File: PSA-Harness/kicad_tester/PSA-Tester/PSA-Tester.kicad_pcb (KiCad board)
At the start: 2 copper layers, 35 parts, among them J11 USB_C_Receptacle, SW1 SW_Push, SW2 SW_Push, SW3 SW_Push, U1 MCP23017_SO, U10 ESP32-C3-OLED, U2 MCP23017_SO, U3 MCP23017_SO, U4 MCP23017_SO, U5 MCP23017_SO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

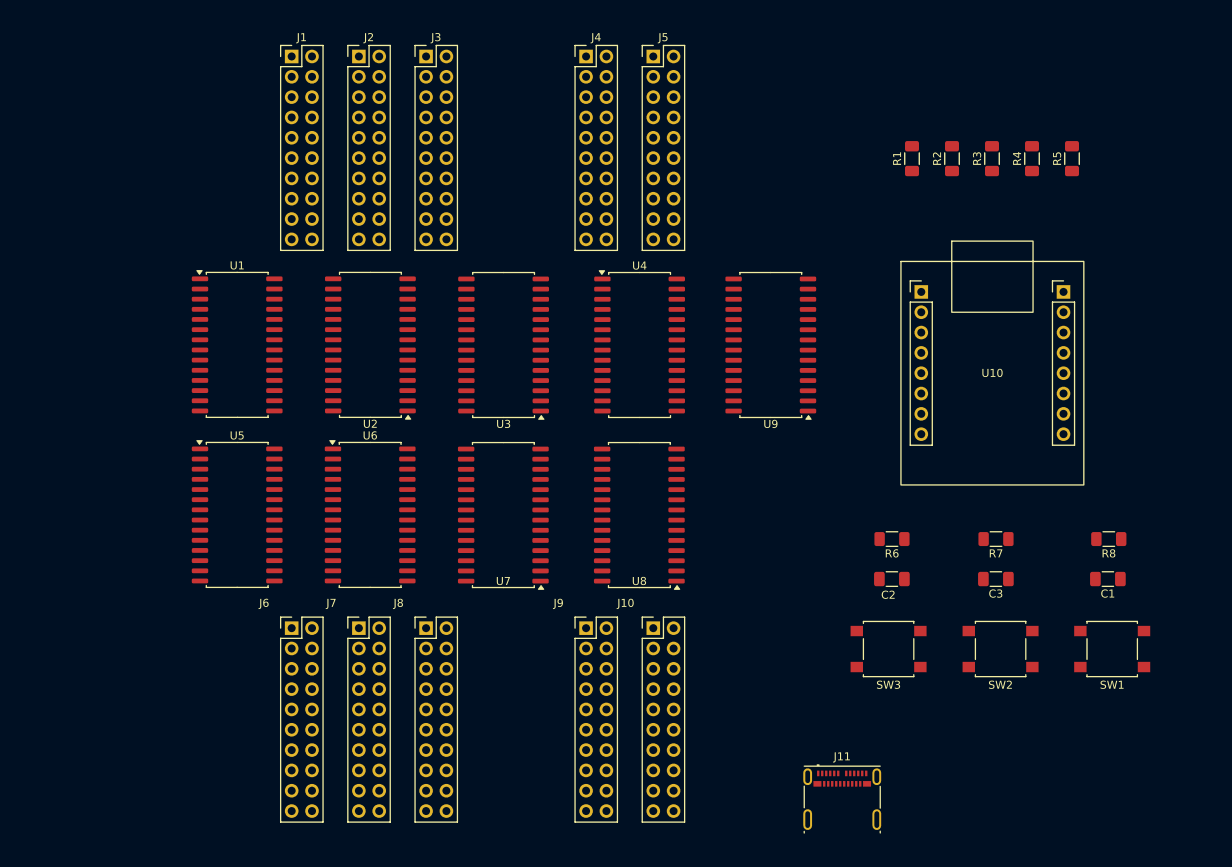
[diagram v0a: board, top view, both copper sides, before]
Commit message: swap mux footprint to DIP-28
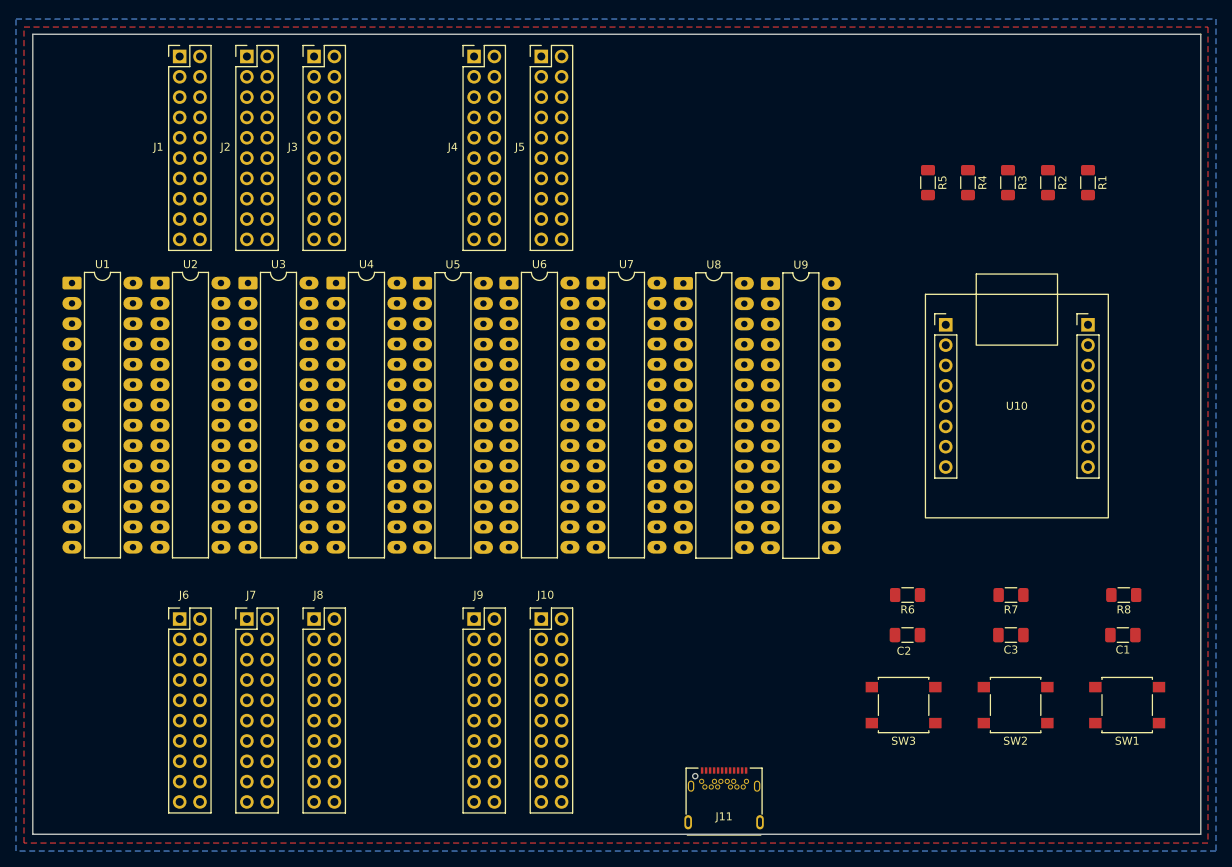
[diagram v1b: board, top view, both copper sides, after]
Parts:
- J11: footprint Connector_USB:USB_C_Receptacle_Molex_105450-0101 -> 0_tester:TYPE-C-31-M-04
- U1, U2, U3, U4, U5, U6, U7, U8, U9: footprint Package_SO:SOIC-28W_7.5x17.9mm_P1.27mm -> Package_DIP:CERDIP-28_W7.62mm_SideBrazed_LongPads
- moved U4 38.7 mm to (77.0, 74.0)
- moved U5 37.1 mm to (87.8, 74.0)
- moved U6 33.8 mm to (98.6, 74.0)
- moved U3 32.9 mm to (66.0, 74.0), turned to 0 degrees
- moved U7 31.2 mm to (109.5, 74.0), turned to 0 degrees
- moved U8 29.5 mm to (120.4, 74.0), turned to 0 degrees
- moved U2 27.4 mm to (55.0, 74.0), turned to 0 degrees
- moved R1 22.2 mm to (171.0, 61.5), turned to -90 degrees
- moved U1 22.0 mm to (44.0, 74.0)
- moved R5 18.2 mm to (151.0, 61.5), turned to -90 degrees
- moved J11 14.8 mm to (125.5, 140.0)
- moved J10 14.0 mm to (102.7, 116.0)
- moved J7 14.0 mm to (65.9, 116.0)
- moved J8 14.0 mm to (74.3, 116.0)
- moved J9 14.0 mm to (94.3, 116.0)
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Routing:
- added copper zone on B.Cu, net +3V3
- added copper zone on F.Cu, net GND
- added copper zone on In1.Cu, net GND
- added copper zone on In2.Cu, net GND
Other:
- board outline added: 146 x 100 mm
- copper layers 2 -> 4

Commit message: still 6 unrouted
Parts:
- moved R1 33.2 mm to (138.0, 57.5), turned to 90 degrees
- moved R2 33.2 mm to (133.0, 57.5)
- moved R3 33.2 mm to (128.0, 57.5)
- moved R4 33.2 mm to (123.0, 57.5)
- moved R5 33.2 mm to (118.0, 57.5)
- moved U10 32.2 mm to (149.2, 47.2)
- moved U9 23.9 mm to (155.2, 74.0)
- moved U8 20.8 mm to (141.2, 74.0)
- moved U7 17.7 mm to (127.2, 73.9)
- moved U6 15.6 mm to (114.2, 74.0)
- moved U5 12.4 mm to (100.2, 74.0)
- moved U4 9.19 mm to (86.2, 74.0)
- moved U3 6.19 mm to (72.2, 74.0)
- moved C1 4.92 mm to (171.5, 121.0)
- moved C2 4.92 mm to (144.5, 121.0)
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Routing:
- net SCL1: track 0.00 -> 233.2 mm, vias 0 -> 1
- net nRESET: track 0.00 -> 212.3 mm, vias 0 -> 2
- net SDA1: track 0.00 -> 198.6 mm, vias 0 -> 2
- net 20a: track 0.00 -> 175.4 mm, vias 0 -> 2
- net 4a: track 0.00 -> 127.1 mm, vias 0 -> 1
- net 18a: track 0.00 -> 118.8 mm, vias 0 -> 1
- net 17a: track 0.00 -> 116.5 mm, vias 0 -> 2
- net 34a: track 0.00 -> 115.4 mm, vias 0 -> 1
- net 15a: track 0.00 -> 114.2 mm, vias 0 -> 3
- net 32a: track 0.00 -> 113.3 mm, vias 0 -> 3
- net 9: track 0.00 -> 113.3 mm, vias 0 -> 1
- net 8: track 0.00 -> 112.8 mm, vias 0 -> 3
- net 33a: track 0.00 -> 111.4 mm, vias 0 -> 1
- net 12a: track 0.00 -> 111.3 mm, vias 0 -> 1
- net BUTTON1: track 0.00 -> 109.5 mm, vias 0 -> 2
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
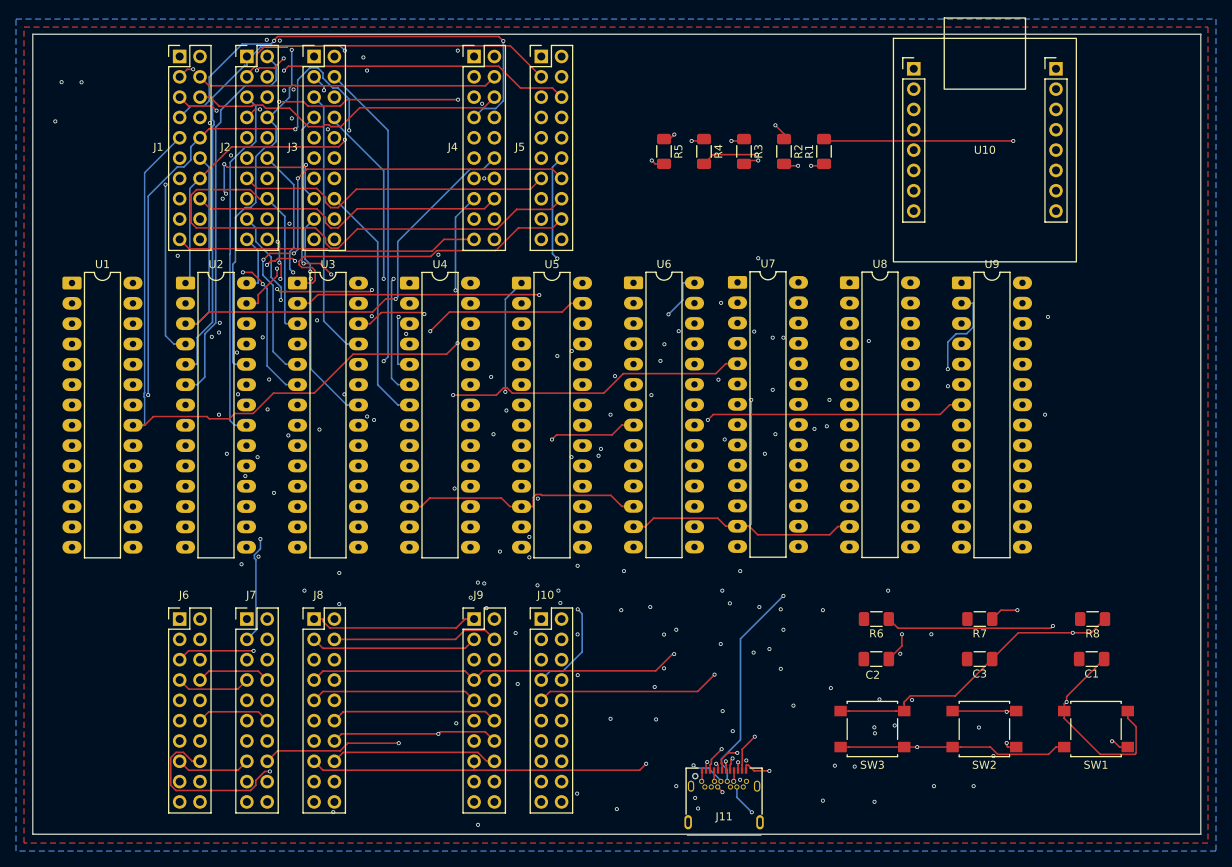
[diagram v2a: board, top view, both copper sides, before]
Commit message: routed with SMD packages
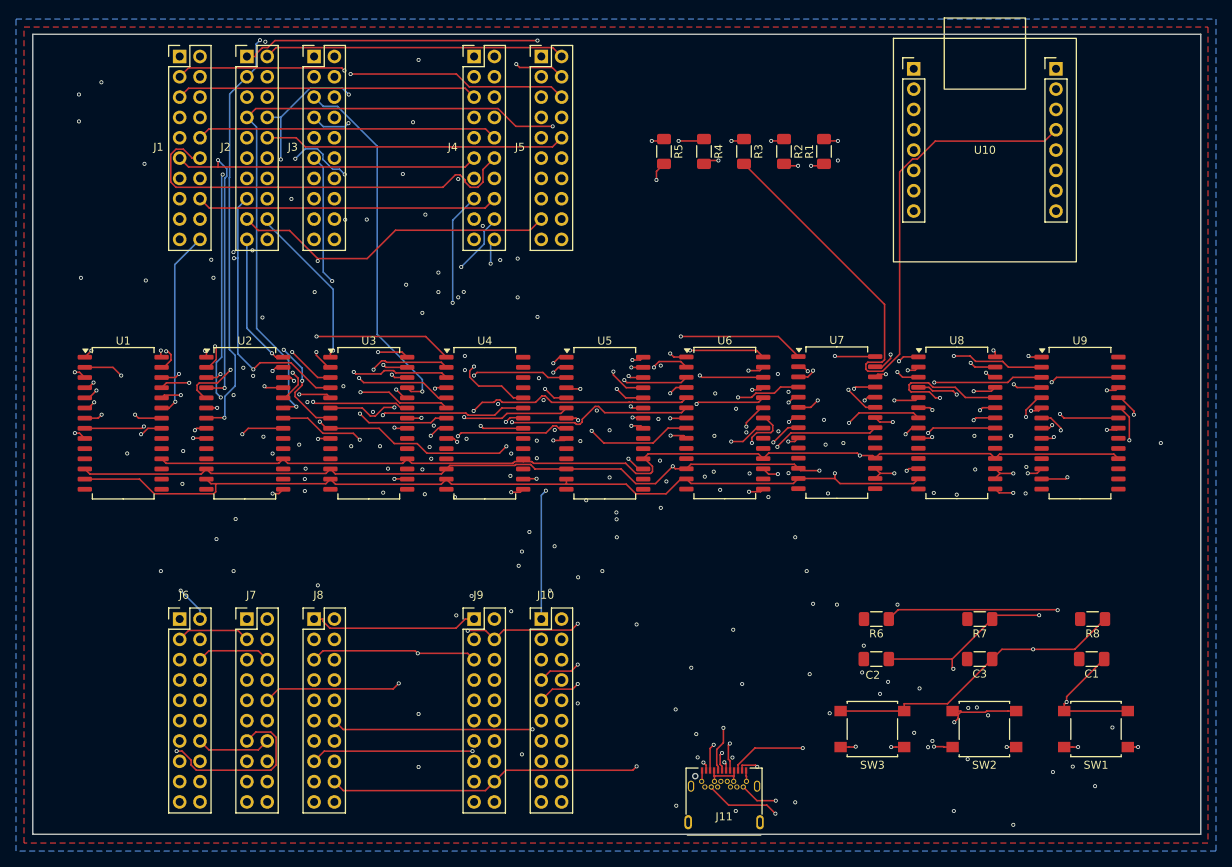
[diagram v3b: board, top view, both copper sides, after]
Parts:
- J11: value USB_C_Receptacle -> U262-241N-4BV60
- SW1, SW2, SW3: value SW_Push -> B3S-1000
- U1, U2, U3, U4, U5, U6, U7, U8, U9: footprint Package_DIP:CERDIP-28_W7.62mm_SideBrazed_LongPads -> Package_SO:SOIC-28W_7.5x18.7mm_P1.27mm
- moved U9 22.9 mm to (170.0, 91.5)
- moved U8 22.1 mm to (154.6, 91.5)
- moved U7 21.5 mm to (139.6, 91.4)
- moved U6 20.9 mm to (125.6, 91.5)
- moved U5 20.4 mm to (110.6, 91.5)
- moved U4 19.9 mm to (95.6, 91.5)
- moved U3 19.7 mm to (81.1, 91.5)
- moved U2 19.0 mm to (65.6, 91.5)
- moved U1 18.7 mm to (50.4, 91.5)
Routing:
- net 20a: track 175.4 -> 100.8 mm
- net 60: track 0.00 -> 52.5 mm, vias 0 -> 3
- net 4a: track 127.1 -> 77.3 mm, vias 1 -> 2
- net 9a: track 89.2 -> 128.0 mm
- net SCL2: track 93.6 -> 131.7 mm
- net 26: track 85.0 -> 122.3 mm, vias 2 -> 3
- net 6: track 94.1 -> 127.9 mm, vias 1 -> 4
- net 9: track 113.3 -> 79.8 mm
- net 1: track 90.1 -> 121.5 mm, vias 5 -> 2
- net SCL1: track 233.2 -> 204.0 mm, vias 1 -> 4
- net 56: track 72.8 -> 45.8 mm, vias 6 -> 3
- net 7: track 106.3 -> 81.2 mm, vias 2 -> 1
- net 18: track 57.9 -> 80.8 mm, vias 0 -> 2
- net 5a: track 88.7 -> 108.3 mm
- net 75: track 76.4 -> 95.4 mm, vias 2 -> 3
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
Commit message: 100x100mm routed
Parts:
- added M1: MountingHole_3.2mm_M3_Pad_Via, MountingHole:MountingHole_3.2mm_M3_Pad_Via, F.Cu at (42.5, 46.4)
- added M2: MountingHole_3.2mm_M3_Pad_Via, MountingHole:MountingHole_3.2mm_M3_Pad_Via, F.Cu at (135.5, 46.4)
- added M3: MountingHole_3.2mm_M3_Pad_Via, MountingHole:MountingHole_3.2mm_M3_Pad_Via, F.Cu at (42.5, 139.4)
- added M4: MountingHole_3.2mm_M3_Pad_Via, MountingHole:MountingHole_3.2mm_M3_Pad_Via, F.Cu at (135.5, 139.4)
- moved U5 63.8 mm to (47.3, 99.8)
- moved U6 63.1 mm to (63.1, 99.8)
- moved U7 61.7 mm to (78.5, 99.8)
- moved U8 61.0 mm to (94.2, 99.8)
- moved U9 60.6 mm to (110.0, 99.8)
- moved C3 57.2 mm to (113.0, 85.0)
- moved R7 57.2 mm to (113.0, 80.0)
- moved C1 55.7 mm to (128.9, 85.0)
- moved R8 55.7 mm to (129.1, 80.0)
- moved SW1 52.6 mm to (128.7, 99.8)
- moved R6 43.0 mm to (121.0, 80.0)
- moved C2 43.0 mm to (121.0, 85.0)
- moved U10 37.5 mm to (111.7, 45.6)
- moved SW2 33.5 mm to (128.8, 113.5)
- moved R1 16.5 mm to (131.0, 72.5)
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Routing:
- net 9a: track 128.0 -> 37.1 mm, vias 2 -> 1
- net 18a: track 134.4 -> 49.2 mm, vias 3 -> 1
- net 5a: track 108.3 -> 40.0 mm, vias 2 -> 1
- net 60a: track 105.6 -> 40.8 mm, vias 3 -> 1
- net 19a: track 109.4 -> 47.7 mm, vias 3 -> 1
- net 59a: track 92.3 -> 32.5 mm, vias 2 -> 1
- net 58a: track 94.1 -> 35.1 mm, vias 2 -> 1
- net 20a: track 100.8 -> 43.7 mm
- net 57a: track 90.0 -> 33.4 mm, vias 3 -> 1
- net 16a: track 109.1 -> 53.5 mm, vias 3 -> 2
- net 76: track 95.5 -> 40.5 mm, vias 3 -> 2
- net SCL2: track 131.7 -> 77.0 mm, vias 1 -> 3
- net 52a: track 102.3 -> 48.7 mm, vias 3 -> 1
- net 77: track 100.1 -> 48.0 mm, vias 2 -> 1
- net 7a: track 93.4 -> 41.9 mm, vias 3 -> 1
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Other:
- board size 146 x 100 mm -> 100 x 100 mm
- board text added: "DOWN"
- board text added: "OK"
- board text added: "UP"

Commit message: part fixes
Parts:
- SW1, SW2, SW3: footprint Button_Switch_SMD:SW_SPST_B3S-1000 -> 0_tester:SW_SPST_B3S-1000
- U1, U2, U3, U4, U5, U6, U7, U8, U9: value MCP23017_SO -> MCP23017T-E/SO
- moved R8 16.0 mm to (113.0, 80.0)
- moved R6 8.00 mm to (129.1, 80.0)
- moved R7 8.00 mm to (121.0, 80.0)
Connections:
- J11 pad S1: (no net) -> 79
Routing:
- net nRESET: track 207.7 -> 0.00 mm, vias 7 -> 0
- net SDA1: track 184.2 -> 0.00 mm, vias 3 -> 0
- net SCL1: track 178.9 -> 0.00 mm, vias 3 -> 0
- net 6: track 123.0 -> 0.00 mm, vias 3 -> 0
- net 8: track 112.9 -> 0.00 mm, vias 1 -> 0
- net 25: track 102.3 -> 0.00 mm, vias 2 -> 0
- net BUTTON3: track 96.6 -> 0.00 mm, vias 3 -> 0
- net SDA2: track 88.6 -> 0.00 mm, vias 2 -> 0
- net 10: track 88.3 -> 0.00 mm, vias 5 -> 0
- net 39: track 84.3 -> 0.00 mm, vias 2 -> 0
- net 4: track 82.3 -> 0.00 mm, vias 3 -> 0
- net 16: track 82.1 -> 0.00 mm, vias 3 -> 0
- net 34a: track 80.6 -> 0.00 mm, vias 1 -> 0
- net 20: track 80.3 -> 0.00 mm, vias 2 -> 0
- net 22: track 77.4 -> 0.00 mm, vias 1 -> 0
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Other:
- board text added: "MEB"
- board text added: "PSA"

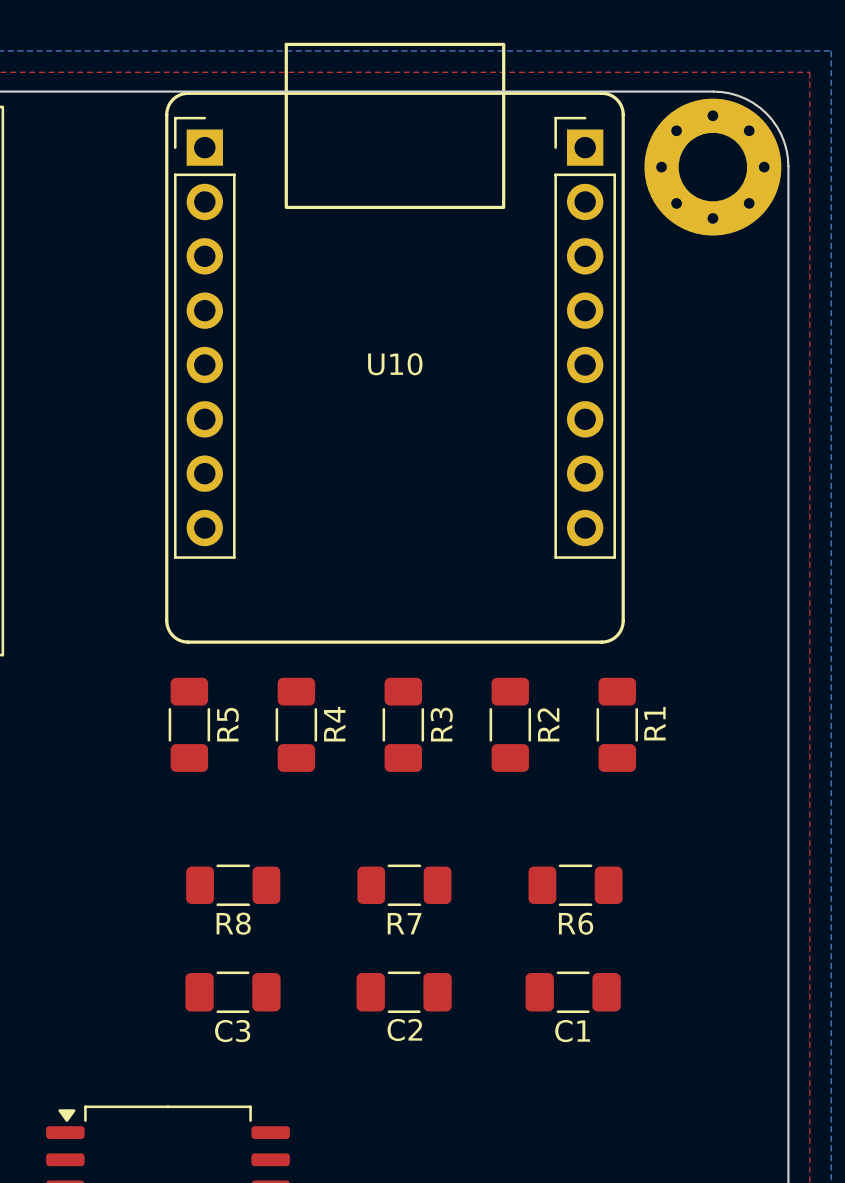
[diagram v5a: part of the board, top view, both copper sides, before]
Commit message: add RGB LED
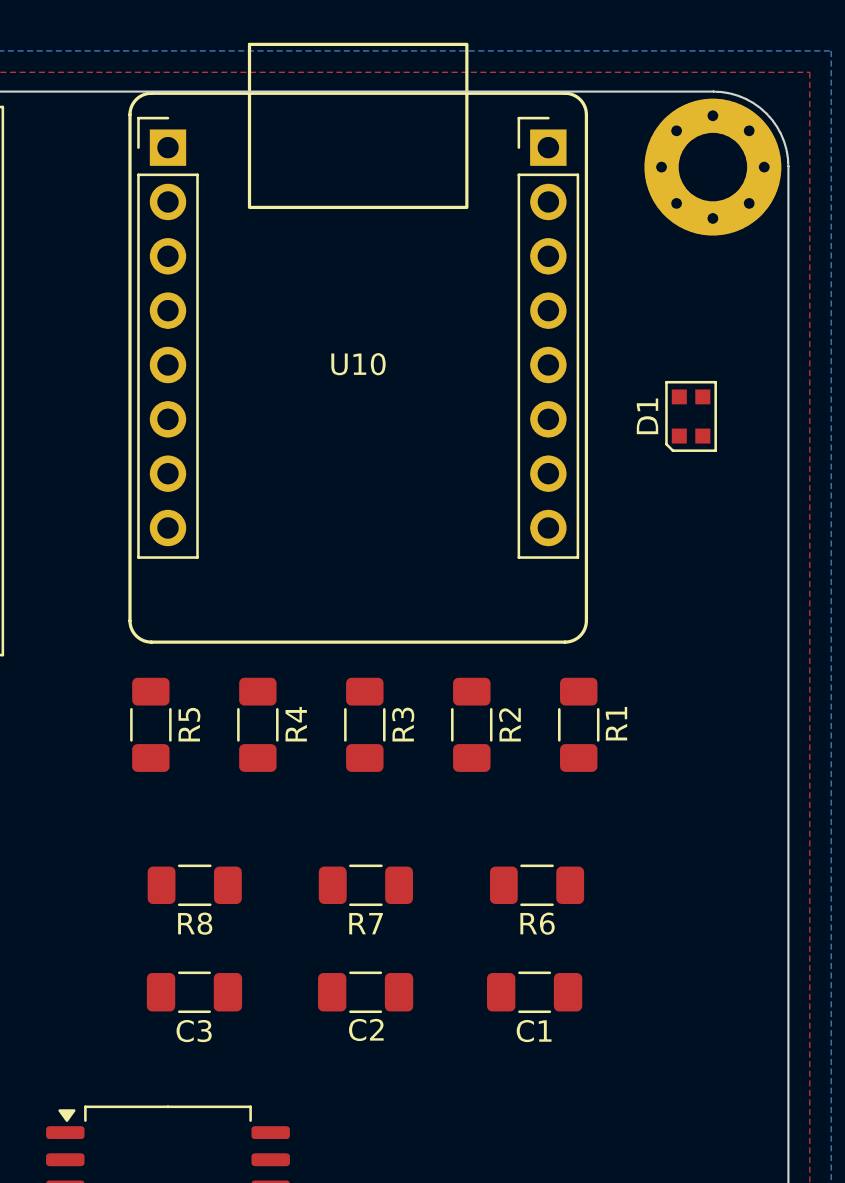
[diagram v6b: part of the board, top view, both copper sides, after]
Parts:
- added D1: WS2812C-2020-V1, 0_tester:LED_WS2812B-2020_PLCC4_2.0x2.0mm, F.Cu at (134.4, 58.1)
- moved R1 1.80 mm to (129.2, 72.5)
- moved R6 1.80 mm to (127.2, 80.0)
- moved C1 1.80 mm to (127.1, 85.0)
- moved C2 1.80 mm to (119.2, 85.0)
- moved C3 1.80 mm to (111.2, 85.0)
- moved R2 1.80 mm to (124.2, 72.5)
- moved R3 1.80 mm to (119.2, 72.5)
- moved R4 1.80 mm to (114.2, 72.5)
- moved R5 1.80 mm to (109.2, 72.5)
- moved R7 1.80 mm to (119.2, 80.0)
- moved R8 1.80 mm to (111.2, 80.0)
- moved U10 1.72 mm to (110.0, 45.5)
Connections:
- U10 pad 2: unconnected-(U10-Pad2) -> Net-(D1-DIN)
- U10 pad 5V: unconnected-(U10-Pad5V) -> +5V

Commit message: add texts
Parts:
- added C4: 10u, Capacitor_SMD:C_1206_3216Metric_Pad1.33x1.80mm_HandSolder, F.Cu at (106.5, 49.2)
- moved C1 13.7 mm to (126.0, 71.4)
- moved C3 13.6 mm to (112.0, 71.4)
- moved C2 13.6 mm to (119.0, 71.4)
- moved R1 10.9 mm to (126.9, 83.2)
- moved R5 10.8 mm to (110.9, 83.2)
- moved R2 10.7 mm to (122.9, 83.2)
- moved R4 10.7 mm to (114.9, 83.2)
- moved R3 10.7 mm to (118.9, 83.2)
- moved R6 4.81 mm to (125.8, 75.4)
- moved R8 4.65 mm to (111.9, 75.4)
- moved R7 4.61 mm to (118.9, 75.4)
- moved D1 0.67 mm to (134.4, 57.4)
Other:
- board text added: "Harness Tester for PSA / VW MEB"
- board text added: "OBD-C"
- board text added: "plug"
- board text added: "socket"

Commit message: partly routed
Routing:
- net SDA1: track 0.00 -> 123.2 mm
- net SCL1: track 0.00 -> 118.8 mm
- net nRESET: track 0.00 -> 112.6 mm
- net BUTTON3: track 0.00 -> 90.6 mm
- net BUTTON2: track 0.00 -> 64.6 mm
- net BUTTON1: track 0.00 -> 43.4 mm
- net SDA2: track 0.00 -> 35.2 mm
- net SCL2: track 0.00 -> 32.3 mm
- net +5V: track 0.00 -> 30.7 mm
- net Net-(D1-DIN): track 0.00 -> 25.7 mm
